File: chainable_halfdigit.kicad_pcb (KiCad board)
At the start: 2 copper layers, 100 x 100 mm, 80 parts, among them J1 Conn_01x03, J2 Conn_01x03, U1 arduino_nano

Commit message: Fixed 5V/GND legend (was inverted)
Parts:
- moved G*** 5.20 mm to (177.4, 59.0)
- moved G*** 2.60 mm to (177.4, 64.2)
- moved G*** 2.60 mm to (177.4, 61.6)
- moved G*** 0.20 mm to (177.4, 63.8)
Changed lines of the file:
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@@
   )
   (module lib_fp:legend_item_round_circled (layer F.Cu)
-    (at 177.4 64)
+    (at 177.4 63.8)
     (fp_text reference G*** (at -10 0) (layer F.SilkS) hide
       (effects (font (size 1.5 1.5) (thickness 0.225)))
@@
   )
   (module lib_fp:legend_item_round_circled (layer B.Cu)
-    (at 177.4 61.6)
+    (at 177.4 64.2)
     (fp_text reference G*** (at -10 0) (layer B.SilkS) hide
       (effects (font (size 1.5 1.5) (thickness 0.225)) (justify mirror))
     )
-    (fp_text value LOGO (at -4.2 -0.2) (layer B.SilkS) hide
+    (fp_text value LOGO (at -6.6 -0.6) (layer B.SilkS) hide
       (effects (font (thickness 0.3)) (justify mirror))
     )
@@
   )
   (module lib_fp:legend_item_round_stripe (layer B.Cu)
-    (at 177.4 64.2)
+    (at 177.4 59)
     (fp_text reference G*** (at -10 -0.4) (layer B.SilkS) hide
       (effects (font (size 1.5 1.5) (thickness 0.225)) (justify mirror))
@@
   )
   (module lib_fp:legend_item_round_plain (layer B.Cu)
-    (at 177.4 59)
+    (at 177.4 61.6)
     (fp_text reference G*** (at -9.8 -0.4) (layer B.SilkS) hide
       (effects (font (size 1.5 1.5) (thickness 0.225)) (justify mirror))

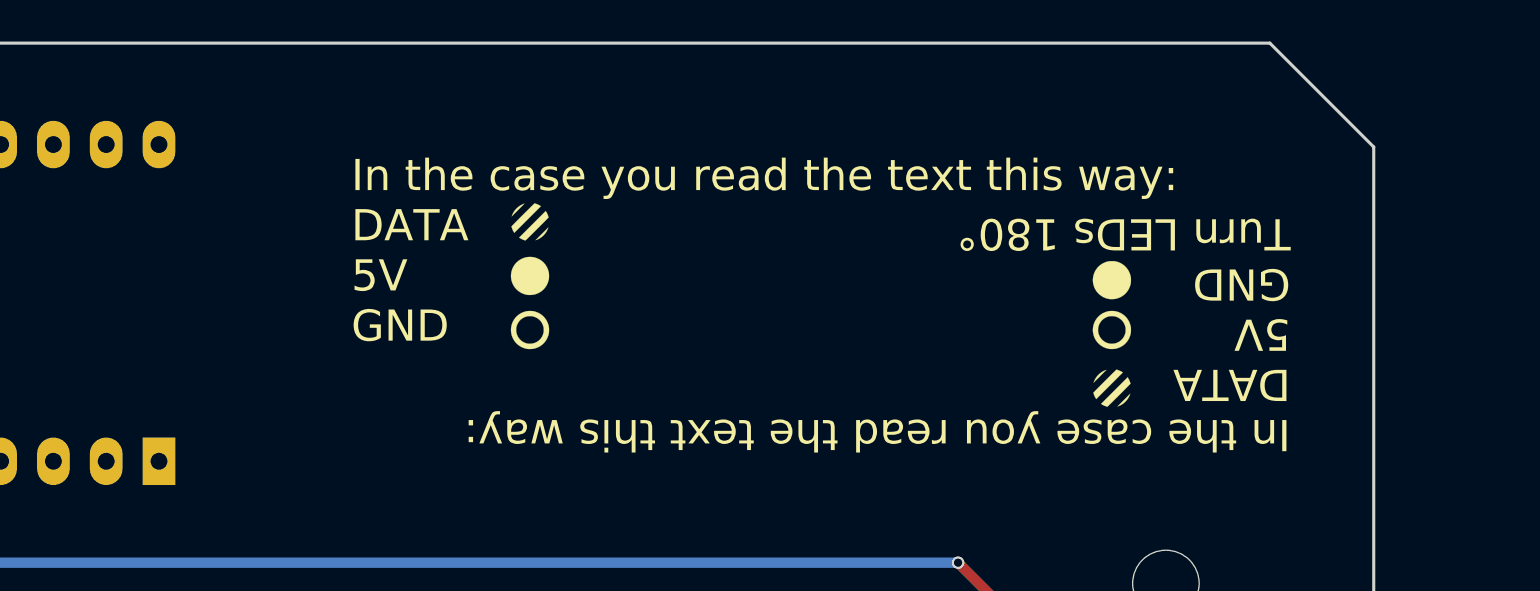
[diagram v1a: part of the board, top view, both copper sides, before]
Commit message: Totated instructions 180°, so controller can be placed bottom right.
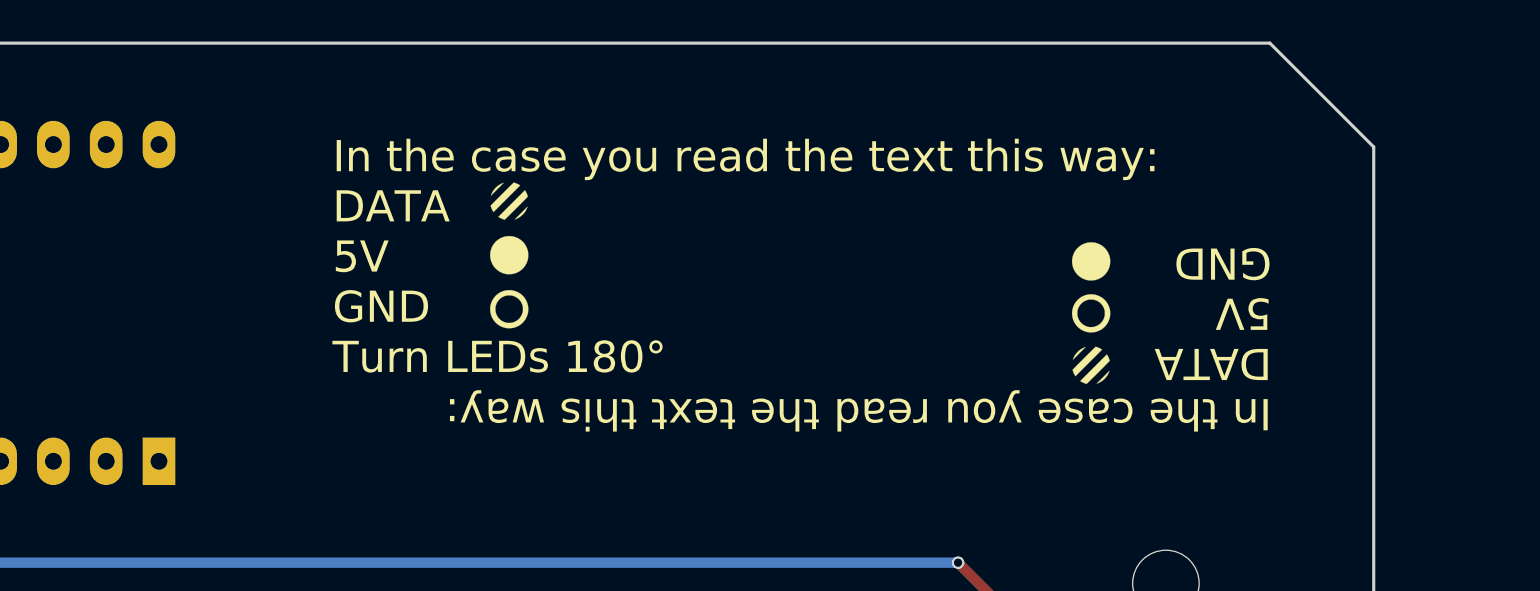
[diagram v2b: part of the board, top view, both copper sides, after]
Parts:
- moved G*** 1.49 mm to (176.4, 65.5)
- moved G*** 1.41 mm to (148.4, 63.4)
- moved G*** 1.41 mm to (148.4, 57.6)
- moved G*** 1.41 mm to (176.4, 63.2)
- moved G*** 1.41 mm to (148.4, 62.8)
- moved G*** 1.41 mm to (176.4, 58.0)
- moved G*** 1.41 mm to (176.4, 60.6)
- moved G*** 1.41 mm to (148.4, 66.0)
- moved G*** 1.41 mm to (148.4, 60.8)
- moved G*** 1.41 mm to (148.4, 60.2)
- moved G*** 1.35 mm to (176.4, 60.5)
- moved G*** 1.28 mm to (176.4, 63.0)
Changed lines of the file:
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@@
     (links 306)
     (no_connects 0)
-    (area 79.824572 49.924999 190.075001 150.477981)
+    (area 89.924999 49.924999 190.075001 150.075001)
     (thickness 1.6)
     (drawings 13)
@@
   (layers
     (0 F.Cu signal)
-    (31 B.Cu signal)
+    (31 B.Cu signal hide)
     (32 B.Adhes user)
     (33 F.Adhes user)
     (34 B.Paste user)
     (35 F.Paste user)
-    (36 B.SilkS user)
+    (36 B.SilkS user hide)
     (37 F.SilkS user)
     (38 B.Mask user)
@@
   )
   (module lib_fp:legend_item_round_stripe (layer F.Cu)
-    (at 149.4 58.6)
+    (at 148.4 57.6)
     (fp_text reference G*** (at 11.4 -0.2) (layer F.SilkS) hide
       (effects (font (size 1.5 1.5) (thickness 0.225)))
@@
   )
   (module lib_fp:legend_item_round_circled (layer F.Cu)
-    (at 149.4 63.8)
+    (at 148.4 62.8)
     (fp_text reference G*** (at 11.6 0) (layer F.SilkS) hide
       (effects (font (size 1.5 1.5) (thickness 0.225)))
@@
   )
   (module lib_fp:legend_item_round_plain (layer F.Cu)
-    (at 149.4 61.2)
+    (at 148.4 60.2)
     (fp_text reference G*** (at 11.2 0) (layer F.SilkS) hide
       (effects (font (size 1.5 1.5) (thickness 0.225)))
@@
   )
   (module lib_fp:legend_item_round_plain (layer F.Cu)
-    (at 177.4 61.4)
+    (at 176.4 60.5)
     (fp_text reference G*** (at -9.8 0.4) (layer F.SilkS) hide
       (effects (font (size 1.5 1.5) (thickness 0.225)))
@@
   )
   (module lib_fp:legend_item_round_stripe (layer F.Cu)
-    (at 177.4 66.6)
+    (at 176.4 65.5)
     (fp_text reference G*** (at -10 0.4) (layer F.SilkS) hide
       (effects (font (size 1.5 1.5) (thickness 0.225)))
@@
   )
   (module lib_fp:legend_item_round_circled (layer F.Cu)
-    (at 177.4 63.8)
+    (at 176.4 63)
     (fp_text reference G*** (at -10 0) (layer F.SilkS) hide
       (effects (font (size 1.5 1.5) (thickness 0.225)))
@@
   )
   (module lib_fp:legend_item_round_circled (layer B.Cu)
-    (at 177.4 64.2)
+    (at 176.4 63.2)
     (fp_text reference G*** (at -10 0) (layer B.SilkS) hide
       (effects (font (size 1.5 1.5) (thickness 0.225)) (justify mirror))
@@
   )
   (module lib_fp:legend_item_round_stripe (layer B.Cu)
-    (at 177.4 59)
+    (at 176.4 58)
     (fp_text reference G*** (at -10 -0.4) (layer B.SilkS) hide
       (effects (font (size 1.5 1.5) (thickness 0.225)) (justify mirror))
@@
   )
   (module lib_fp:legend_item_round_plain (layer B.Cu)
-    (at 177.4 61.6)
+    (at 176.4 60.6)
     (fp_text reference G*** (at -9.8 -0.4) (layer B.SilkS) hide
       (effects (font (size 1.5 1.5) (thickness 0.225)) (justify mirror))
@@
   )
   (module lib_fp:legend_item_round_circled (layer B.Cu)
-    (at 149.4 64.4)
+    (at 148.4 63.4)
     (fp_text reference G*** (at 11.6 0) (layer B.SilkS) hide
       (effects (font (size 1.5 1.5) (thickness 0.225)) (justify mirror))
@@
   )
   (module lib_fp:legend_item_round_stripe (layer B.Cu)
-    (at 149.4 67)
+    (at 148.4 66)
     (fp_text reference G*** (at 11.4 0.2) (layer B.SilkS) hide
       (effects (font (size 1.5 1.5) (thickness 0.225)) (justify mirror))
@@
   )
   (module lib_fp:legend_item_round_plain (layer B.Cu)
-    (at 149.4 61.8)
+    (at 148.4 60.8)
     (fp_text reference G*** (at 11.2 0) (layer B.SilkS) hide
       (effects (font (size 1.5 1.5) (thickness 0.225)) (justify mirror))
@@
     (effects (font (size 1.5 1.5) (thickness 0.3)))
   )
-  (gr_text "In the case you read the text this way:\nDATA\n5V\nGND" (at 140.8 60) (layer F.SilkS)
+  (gr_text "In the case you read the text this way:\nDATA\n5V\nGND" (at 185.1 64.2 180) (layer F.SilkS)
     (effects (font (size 1.5 1.5) (thickness 0.3)) (justify left))
   )
-  (gr_text "In the case you read the text this way:\nDATA\n5V\nGND\nTurn LEDs 180°" (at 186 64 180) (layer F.SilkS)
+  (gr_text "In the case you read the text this way:\nDATA\n5V\nGND\nTurn LEDs 180°" (at 139.9 60.3 360) (layer F.SilkS)
     (effects (font (size 1.5 1.5) (thickness 0.3)) (justify left))
   )
-  (gr_text "In the case you read the text this way:\nDATA\n5V\nGND\nTurn LEDs 180°" (at 140.8 64.4 180) (layer B.SilkS)
+  (gr_text "In the case you read the text this way:\nDATA\n5V\nGND\nTurn LEDs 180°" (at 185 60.6 360) (layer B.SilkS)
     (effects (font (size 1.5 1.5) (thickness 0.3)) (justify left mirror))
   )
-  (gr_text "In the case you read the text this way:\nDATA\n5V\nGND" (at 186 60.4) (layer B.SilkS)
+  (gr_text "In the case you read the text this way:\nDATA\n5V\nGND" (at 139.8 64.6 180) (layer B.SilkS)
     (effects (font (size 1.5 1.5) (thickness 0.3)) (justify left mirror))
   )
